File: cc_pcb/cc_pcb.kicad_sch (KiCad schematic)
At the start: 42 parts, among them J1 Conn_02x05_Odd_Even, SW1 SW_Push, U1 LD1117S33TR_SOT223, U2 STM32F091RCTx

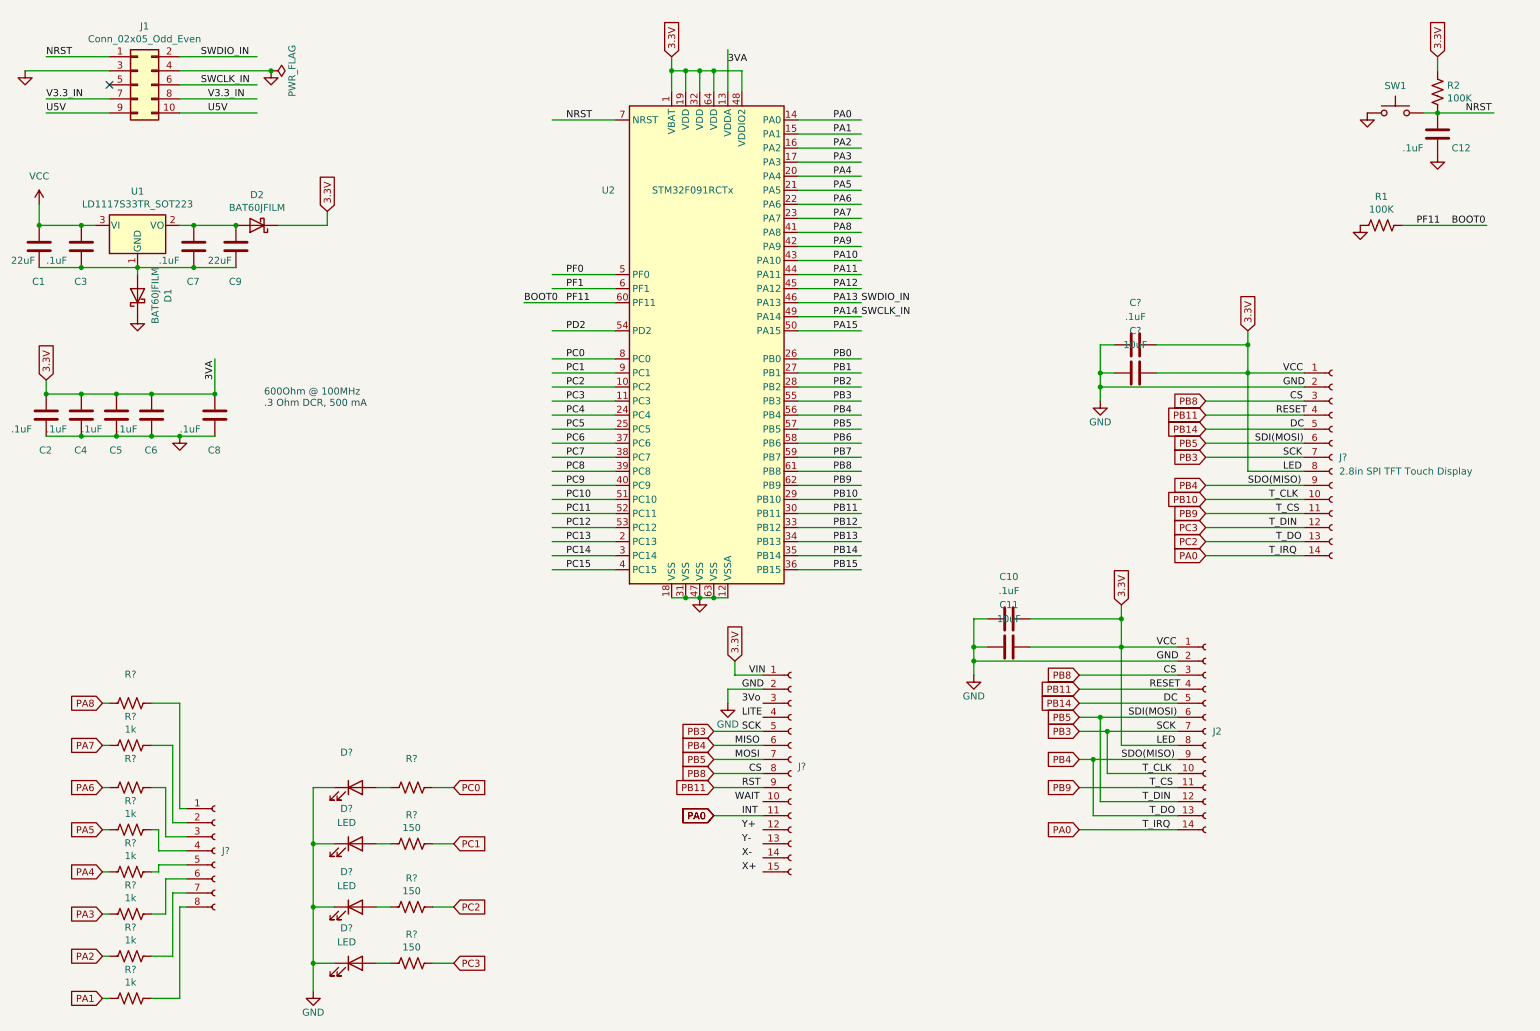
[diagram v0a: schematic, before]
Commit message: SPI-40Pin controller touch added and keypad mod in pcb schematic
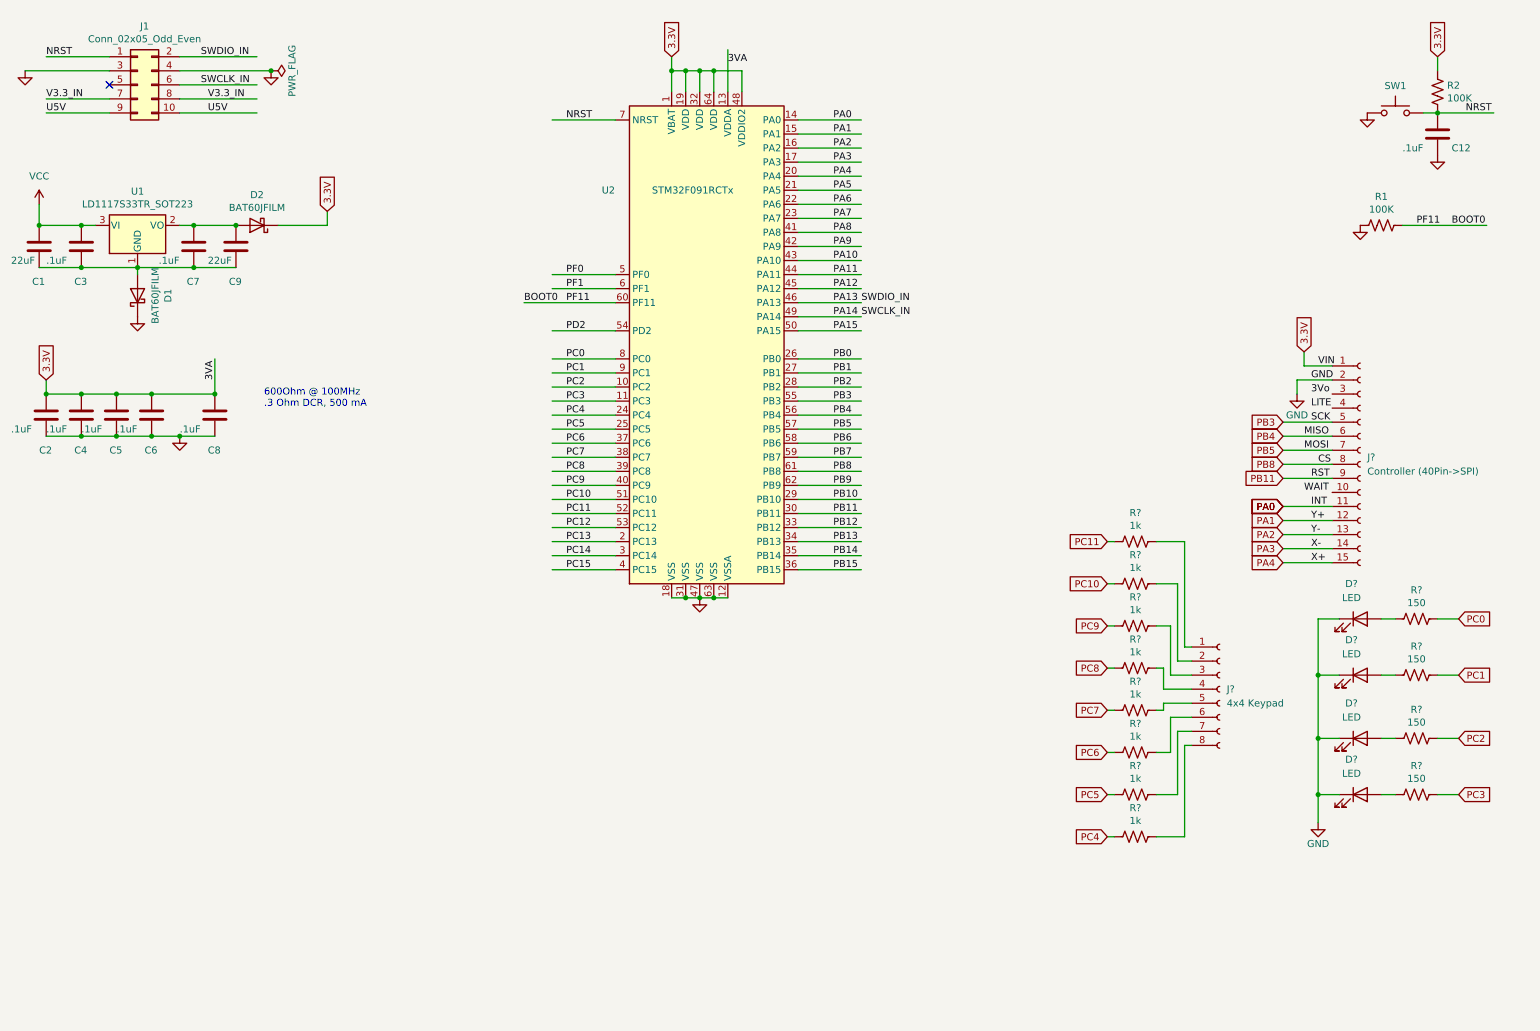
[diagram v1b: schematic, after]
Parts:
- removed C10, C?: .1uF, symbol Device:C
- removed C11, C?: 10uF, symbol Device:C
- removed J2: (no value), symbol Connector:Conn_01x14_Female
- removed J?: 2.8in SPI TFT Touch Display, symbol Connector:Conn_01x14_Female
- D?: value (none) -> LED
- J?: value (none) -> Controller (40Pin->SPI)
- J?: value (none) -> 4x4 Keypad
- R? (x2): value (none) -> 1k
- R?: value (none) -> 150
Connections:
- net PA1: now also J?.12 (Pin_12); no longer R?.2
- net PA2: now also J?.13 (Pin_13); no longer R?.2
- net PA3: now also J?.14 (Pin_14); no longer R?.2
- net PA4: now also J?.15 (Pin_15); no longer R?.2
- net PA5: no longer R?.2
- net PA6: no longer R?.2
- net PA7: no longer R?.2
- net PA8: no longer R?.2
- net PB10: no longer J?.5 (Pin_5), U2.55 (PB3)
- net PB4: no longer R?.1, U2.10 (PC2)
- net PB5: no longer R?.1, U2.11 (PC3)
- net PC10: now also R?.2
- net PC11: now also R?.2
- net PC4: now also R?.2
- net PC5: now also R?.2
- net PC6: now also R?.2
- net PC7: now also R?.2
- net PC8: now also R?.2
- net PC9: now also R?.2
- net VCC: no longer C2.1, C4.1, C5.1, C6.1, C8.1, D2.1 (K), J?.1 (Pin_1), R2.1, U2.1 (VBAT), U2.13 (VDDA), U2.19 (VDD), U2.32 (VDD), U2.48 (VDDIO2), U2.64 (VDD)
- new net 3.3V: C2.1, C4.1, C5.1, C6.1, C8.1, D2.1 (K), J?.1 (Pin_1), R2.1, U2.1 (VBAT), U2.13 (VDDA), U2.19 (VDD), U2.32 (VDD), U2.48 (VDDIO2), U2.64 (VDD)
- new net PB3: J?.5 (Pin_5), U2.55 (PB3)
- new net PC2: R?.1, U2.10 (PC2)
- new net PC3: R?.1, U2.11 (PC3)
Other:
- moved on the sheet: D?, J?, R?

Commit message: wi-fi module, RFID scanner, sineToSquare converter, AC-DC converter
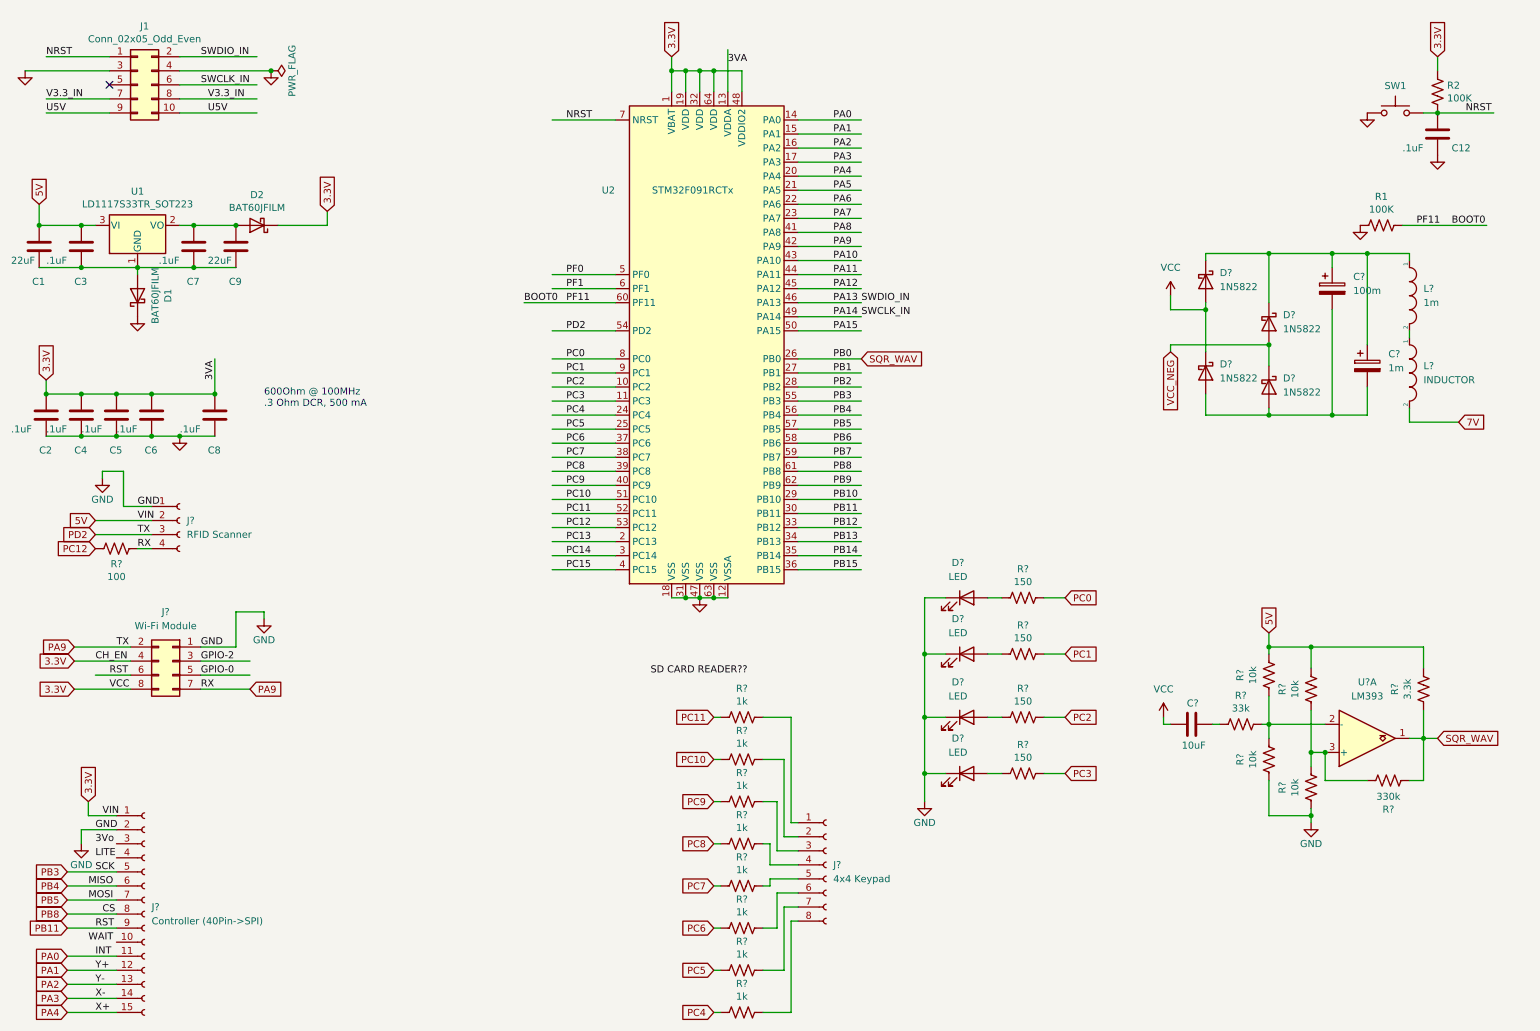
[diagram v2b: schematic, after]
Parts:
- added C?: 10uF, Capacitor_SMD:C_0805_2012Metric_Pad1.18x1.45mm_HandSolder, symbol Device:C
- added C?: 100m, symbol Device:C_Polarized
- added C?: 1m, symbol Device:C_Polarized
- added D? (x4): 1N5822, imported_footprints:DIO_1N5822, symbol Device:D_Schottky
- added J?: RFID Scanner, symbol Connector:Conn_01x04_Female
- added J?: Wi-Fi Module, symbol Connector_Generic:Conn_02x04_Odd_Even
- added L?: 1m, symbol pspice:INDUCTOR
- added L?: INDUCTOR, symbol pspice:INDUCTOR
- added R?: 3.3k, Resistor_SMD:R_0805_2012Metric_Pad1.20x1.40mm_HandSolder, symbol Device:R_US
- added R?: 330k, Resistor_SMD:R_0805_2012Metric_Pad1.20x1.40mm_HandSolder, symbol Device:R_US
- added R? (x4): 10k, Resistor_SMD:R_0805_2012Metric_Pad1.20x1.40mm_HandSolder, symbol Device:R_US
- added R?: 33k, Resistor_SMD:R_0805_2012Metric_Pad1.20x1.40mm_HandSolder, symbol Device:R_US
- added R?: 100, Resistor_SMD:R_0805_2012Metric_Pad1.20x1.40mm_HandSolder, symbol Device:R_US
- added U?: LM393, symbol Comparator:LM393
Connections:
- net 3.3V is gone; now on net VCC: C2.1, C4.1, C5.1, C6.1, C8.1, D2.1 (K), J?.1 (Pin_1), R2.1, U2.1 (VBAT), U2.13 (VDDA), U2.19 (VDD), U2.32 (VDD), U2.48 (VDDIO2), U2.64 (VDD)
- net PD2 is gone; now on net PA9: U2.54 (PD2)
- net GND: now also J?.1 (Pin_1), J?.1 (Pin_1), R?.2, R?.2
- net PA9: now also J?.2 (Pin_2), J?.3 (Pin_3), J?.4 (Pin_4), J?.7 (Pin_7), R?.1
- net PB11: now also J?.6 (Pin_6)
- net PC12: now also R?.2
- net VCC: now also C?.1, D?.1 (K), D?.2 (A), J?.2 (Pin_2), J?.4 (Pin_4), J?.8 (Pin_8), R?.1, R?.1, R?.1
- net PB0 renamed SQR_WAV
- net SQR_WAV: now also R?.2, R?.2, U?.1
- new net: C?.1, C?.1, D?.1 (K), D?.1 (K), L?.1
- new net: L?.1, L?.2
- new net: C?.2, R?.2
- new net: R?.1, R?.1, R?.2, U?.3 (+)
- new net: R?.1, R?.1, R?.2, U?.2 (-)
- new net: C?.2, C?.2, D?.2 (A), D?.2 (A)
- new net 7V: L?.2
- new net GPIO-0: J?.5 (Pin_5)
- new net GPIO-2: J?.3 (Pin_3)
- new net VCC_NEG: D?.1 (K), D?.2 (A)
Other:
- moved on the sheet: D?, J?, R?

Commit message: SD Card Reader Schematic
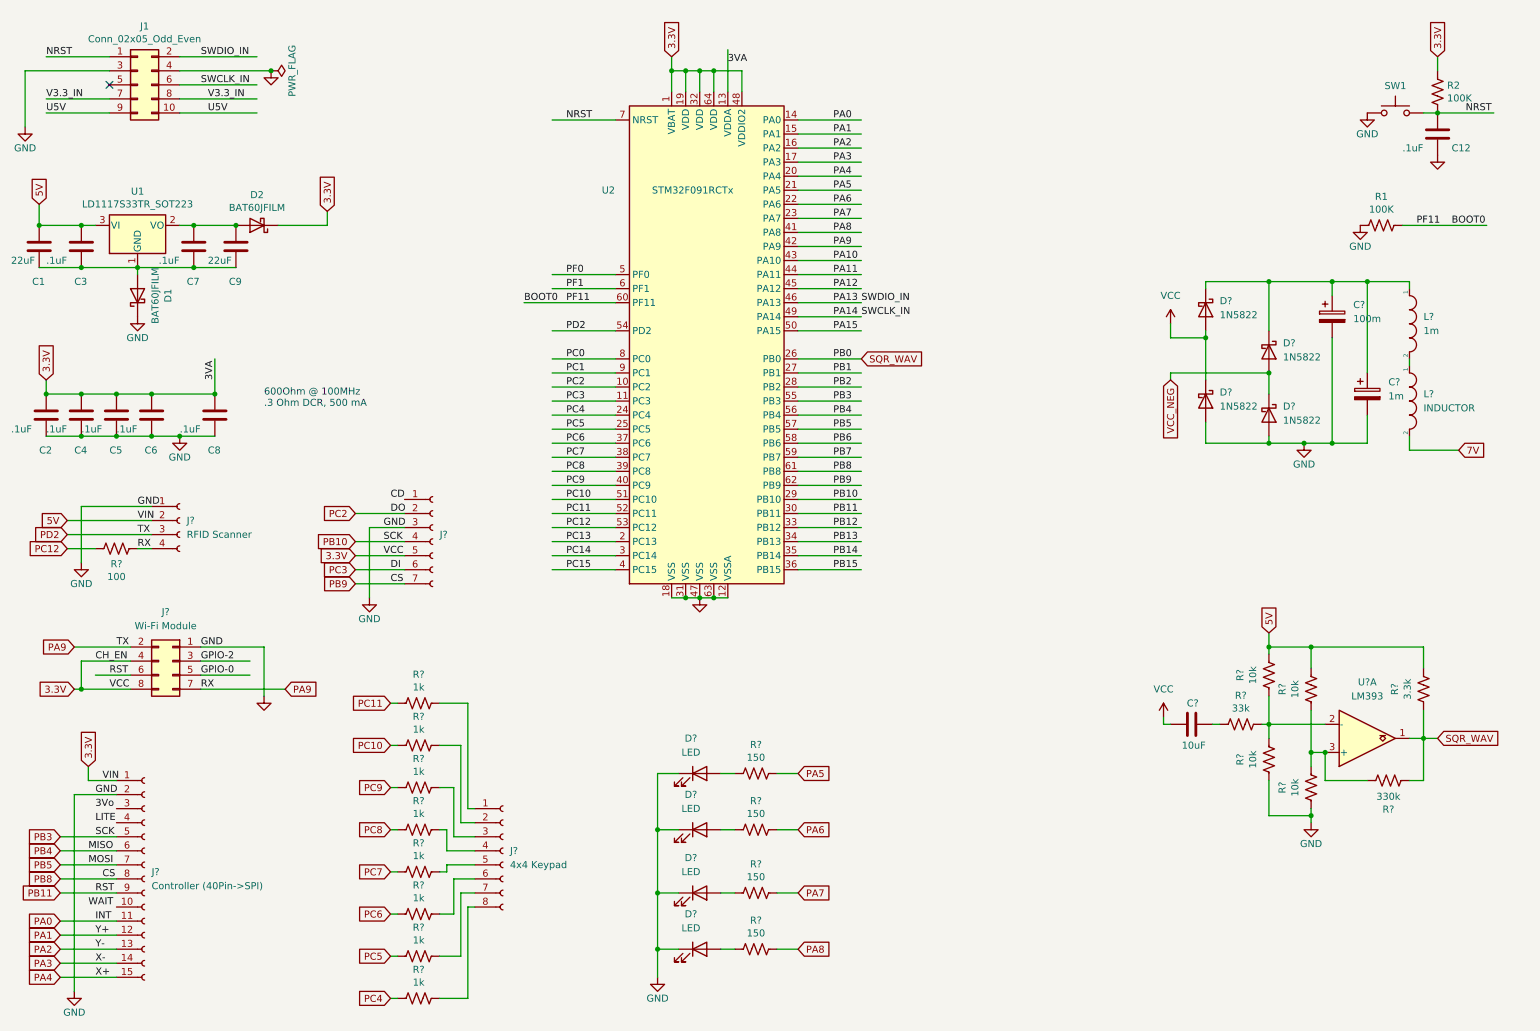
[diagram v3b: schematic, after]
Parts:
- added J?: (no value), symbol Connector:Conn_01x07_Female
- J?: footprint (none) -> imported_footprints:RA8875_TFT_Breakout
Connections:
- net PB3 is gone; now on net PB10: J?.5 (Pin_5), U2.55 (PB3)
- net PB9 is gone; now on net PB8: U2.62 (PB9)
- net GND: now also C?.2, C?.2, D?.2 (A), D?.2 (A), J?.3 (Pin_3)
- net PA5: now also R?.1
- net PA6: now also R?.1
- net PA7: now also R?.1
- net PA8: now also R?.1
- net PB10: now also J?.4 (Pin_4)
- net PB8: now also J?.7 (Pin_7)
- net PC0: no longer R?.1
- net PC1: no longer R?.1
- net PC2: now also J?.2 (Pin_2); no longer R?.1
- net PC3: now also J?.6 (Pin_6); no longer R?.1
- net VCC: now also J?.5 (Pin_5)
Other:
- moved on the sheet: C?, D?, J?, L?, R?
